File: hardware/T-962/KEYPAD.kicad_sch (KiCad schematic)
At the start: 10 parts

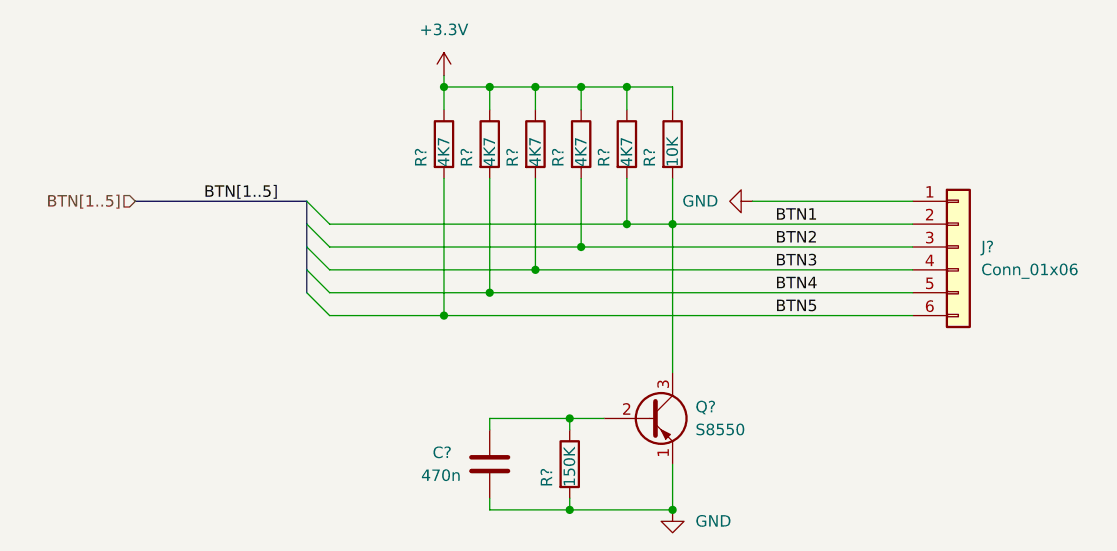
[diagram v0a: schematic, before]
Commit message: fill out designators
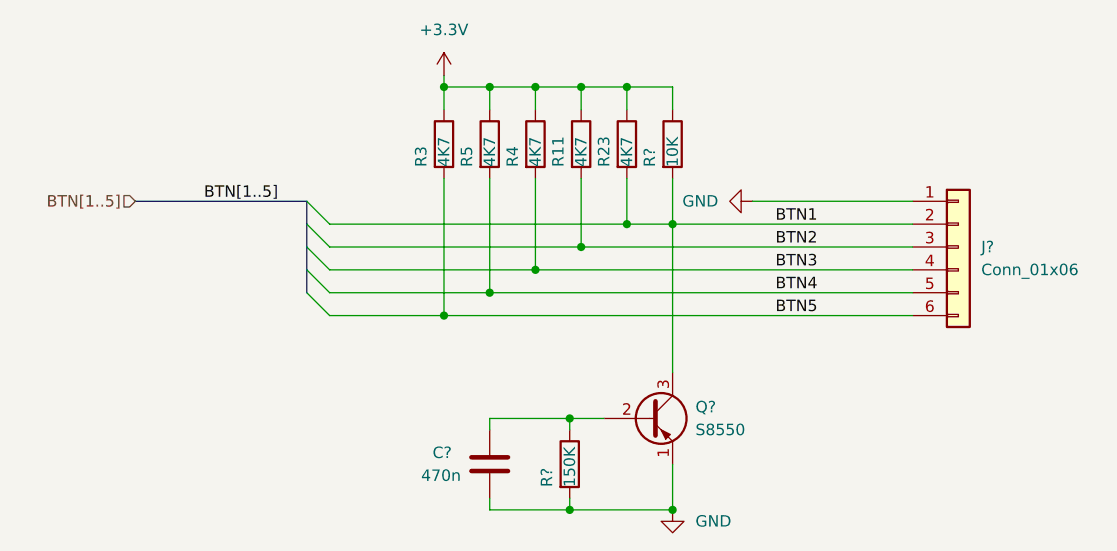
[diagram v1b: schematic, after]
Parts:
- gave numbers to parts that had none: 5
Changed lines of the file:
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@@
   (symbol (lib_id "Device:R") (at 111.76 90.17 0) (unit 1)
     (in_bom yes) (on_board yes)
-    (property "Reference" "R?" (id 0) (at 109.22 92.71 90)
+    (property "Reference" "R3" (id 0) (at 109.22 92.71 90)
       (effects (font (size 1.27 1.27)) (justify left))
     )
@@
   (symbol (lib_id "Device:R") (at 127 90.17 0) (unit 1)
     (in_bom yes) (on_board yes)
-    (property "Reference" "R?" (id 0) (at 124.46 92.71 90)
+    (property "Reference" "R11" (id 0) (at 124.46 92.71 90)
       (effects (font (size 1.27 1.27)) (justify left))
     )
@@
   (symbol (lib_id "Device:R") (at 132.08 90.17 0) (unit 1)
     (in_bom yes) (on_board yes)
-    (property "Reference" "R?" (id 0) (at 129.54 92.71 90)
+    (property "Reference" "R23" (id 0) (at 129.54 92.71 90)
       (effects (font (size 1.27 1.27)) (justify left))
     )
@@
   (symbol (lib_id "Device:R") (at 116.84 90.17 0) (unit 1)
     (in_bom yes) (on_board yes)
-    (property "Reference" "R?" (id 0) (at 114.3 92.71 90)
+    (property "Reference" "R5" (id 0) (at 114.3 92.71 90)
       (effects (font (size 1.27 1.27)) (justify left))
     )
@@
   (symbol (lib_id "Device:R") (at 121.92 90.17 0) (unit 1)
     (in_bom yes) (on_board yes)
-    (property "Reference" "R?" (id 0) (at 119.38 92.71 90)
-      (effects (font (size 1.27 1.27)) (justify left))
-    )
+    (property "Reference" "R4" (id 0) (at 119.38 92.71 90)
+      (effects (font (size 1.27 1.27)) (justify left))
+    )
